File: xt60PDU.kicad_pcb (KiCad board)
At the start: 2 copper layers, 50 x 16 mm, 7 parts, among them J1 Conn_01x02_Pin, J2 Conn_01x02_Socket, J3 Conn_01x02_Socket, J4 Conn_01x02_Socket, J5 Conn_01x02_Socket

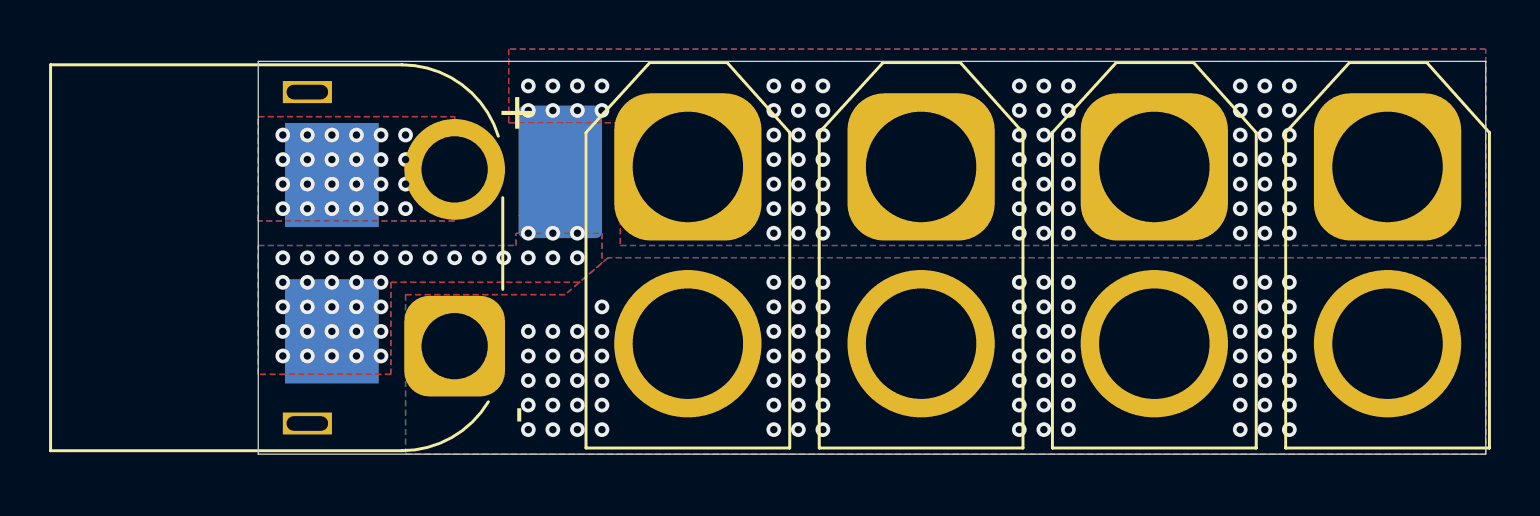
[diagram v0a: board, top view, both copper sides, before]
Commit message: Add v1.0 with fixed pin numbering and connector orientation
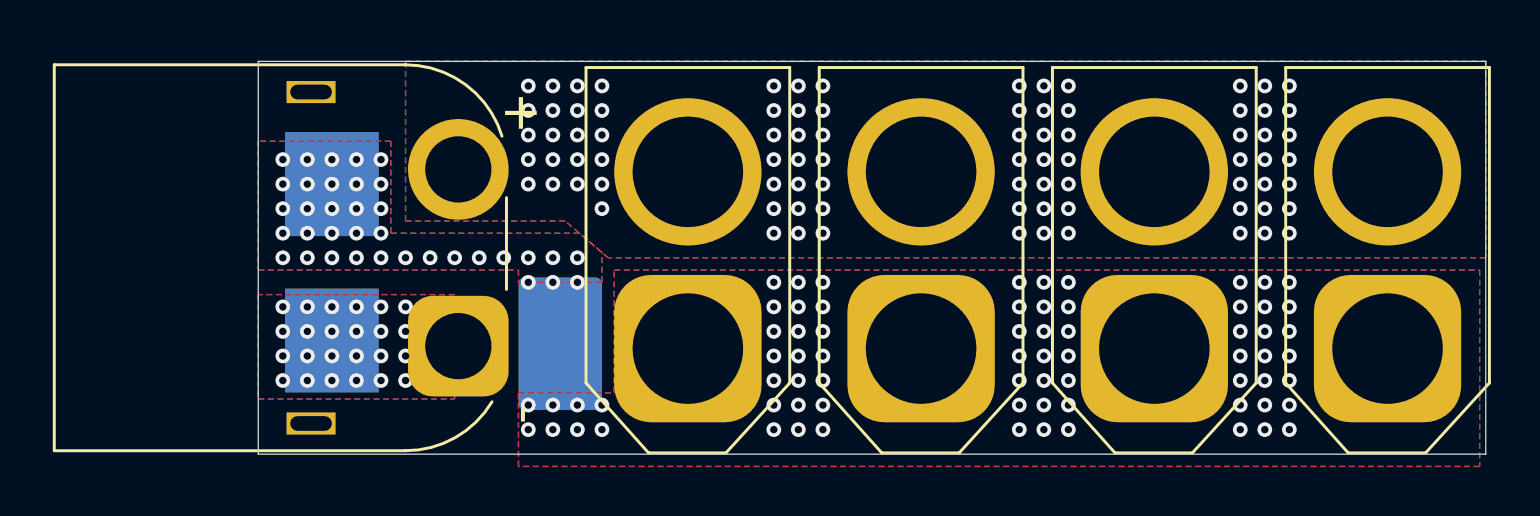
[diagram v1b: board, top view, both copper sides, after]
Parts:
- moved J2 7.40 mm to (67.5, 61.7), turned to 90 degrees
- moved J3 7.40 mm to (77.0, 61.7), turned to 90 degrees
- moved J4 7.40 mm to (86.5, 61.7), turned to 90 degrees
- moved J5 7.40 mm to (96.0, 61.7), turned to 90 degrees
- moved F2 7.00 mm to (62.3, 61.5), turned to -90 degrees
- moved F1 0.37 mm to (53.0, 58.2), turned to -90 degrees
- moved J1 0.15 mm to (58.1, 61.6)
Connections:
- J1 pad 1: /GND -> /VBAT
- J1 pad 2: /VBAT -> /GND
